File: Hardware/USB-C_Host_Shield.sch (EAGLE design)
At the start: 37 parts, among them U1 ARDUINO_UNO_R3_SHIELDBASIC, U3 74HC4050, U5 MAX3421, U6 3.3V/150mA

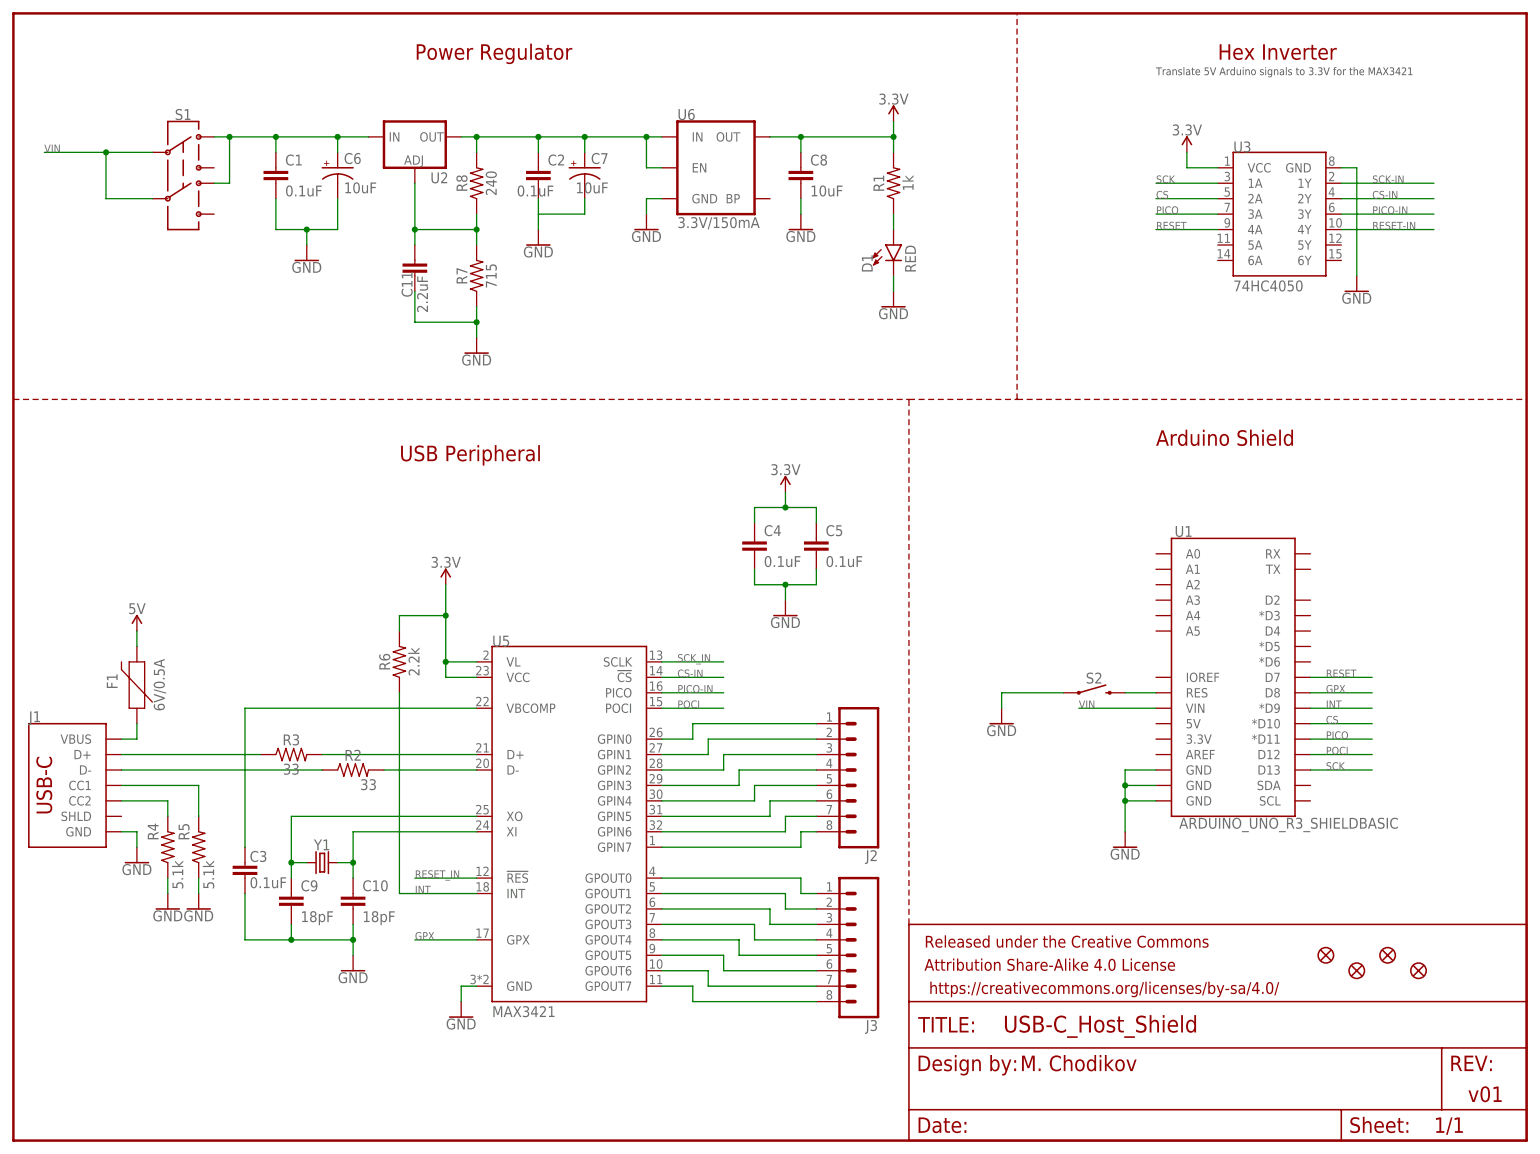
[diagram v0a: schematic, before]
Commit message: Continued with Layout
Adjusted resistors and components to all be 0603 size (besides caps with dielectrics). Placed components in sections so all capacitors and other components are in the right areas.
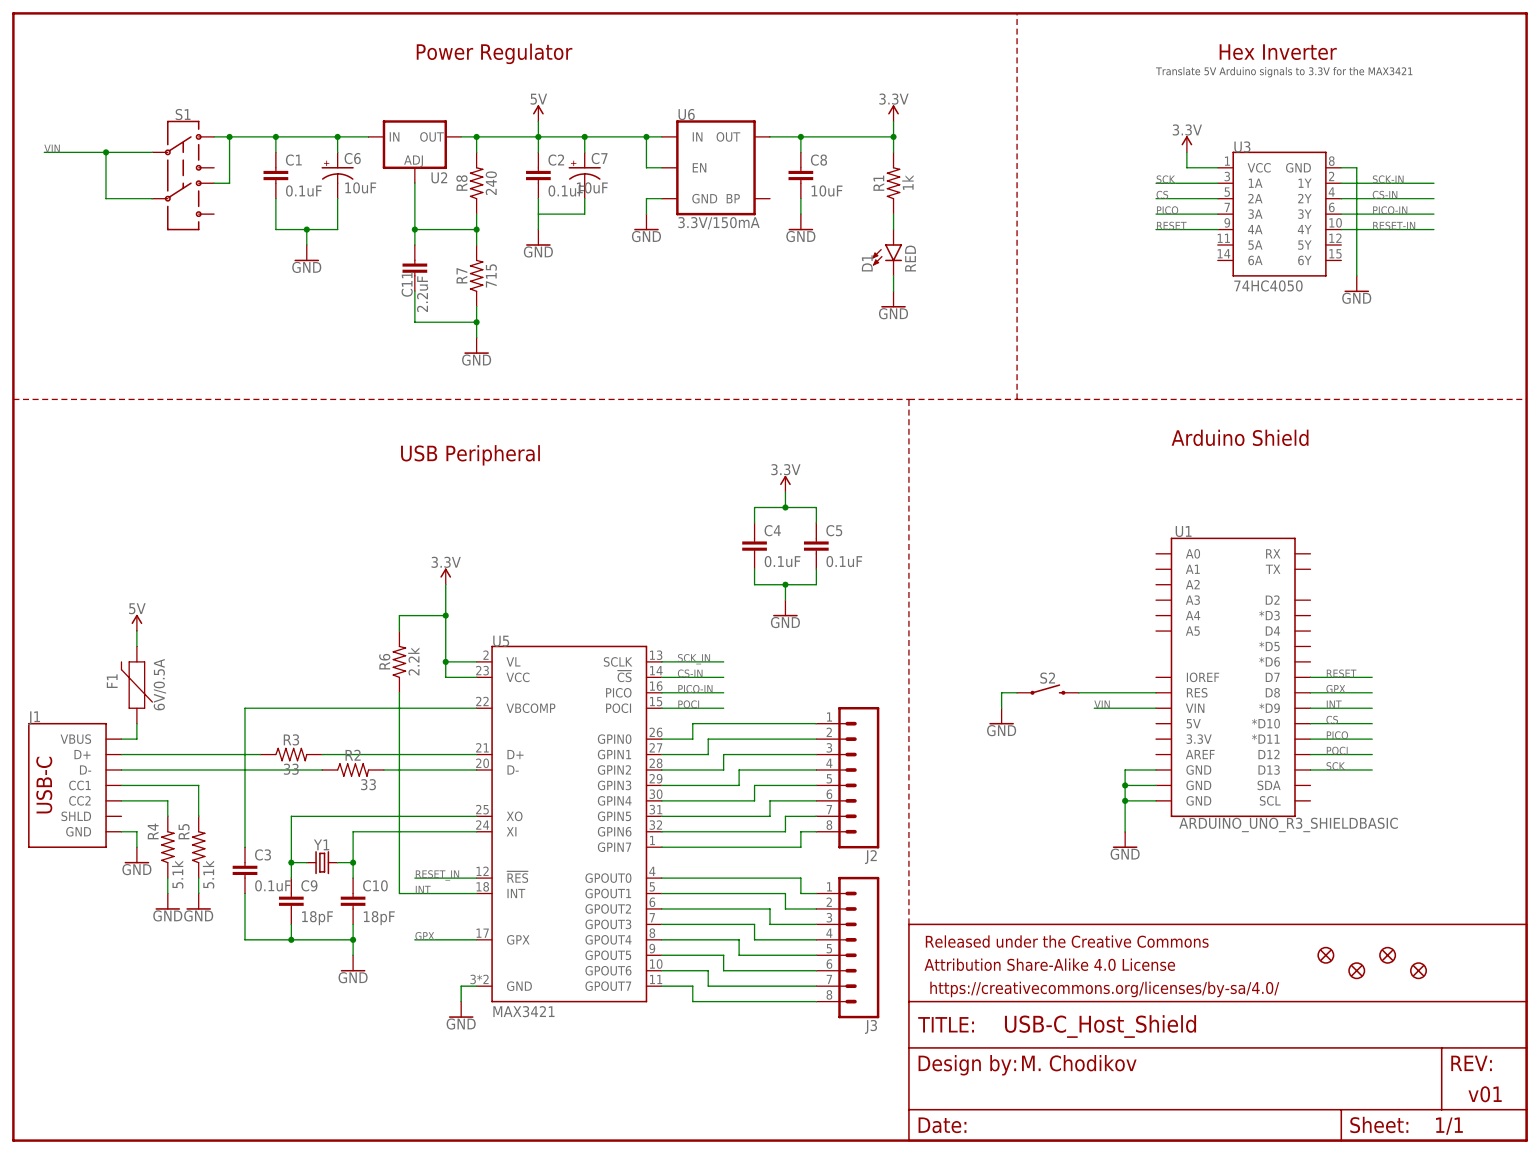
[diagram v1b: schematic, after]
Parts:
- C1, C2, C3, C4, C5: device SparkFun-Capacitors:0.1UF-0402T-6.3V-10%-X7R -> SparkFun-Capacitors:0.1UF-0603-25V-(+80/-20%)
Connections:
- net N$1 renamed D+
- net N$10 renamed MAX_D+
- net N$11 renamed D-
- net N$12 renamed GPOUT0
- net N$13 renamed GPOUT1
- net N$14 renamed GPOUT2
- net N$15 renamed CC1
- net N$16 renamed CC2
- net N$17 renamed GPOUT3
- net N$18 renamed GPOUT4
- net N$19 renamed GPOUT5
- net N$20 renamed GPOUT6
- net N$21 renamed GPOUT7
- net N$22 renamed GPIN7
- net N$23 renamed GPIN6
- net N$24 renamed GPIN5
- net N$25 renamed GPIN4
- net N$26 renamed GPIN3
- net N$27 renamed GPIN2
- net N$28 renamed GPIN1
- net N$29 renamed GPIN0
- net N$31 renamed VBUS
- net N$34 renamed XO
- net N$36 renamed XI
- net N$37 renamed VBCOMP
- net N$9 renamed MAX_D-
- removed net N$3: C2.1, C7.+, R8.2, U2.OUT, U6.EN, U6.IN
- net 5V: now also C2.1, C7.+, R8.2, U2.OUT, U6.EN, U6.IN
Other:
- moved on the sheet: S2

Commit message: Updated for Diff Pair Routing
Updated the layer stackup and net classes for differential pair routing. Changed in both schematic and layout. Routed sensitive signals
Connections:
- net D+ renamed D_P
- net D- renamed D_N
- net MAX_D+ renamed MAX_D_P
- net MAX_D- renamed MAX_D_N
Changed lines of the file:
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@@
 <class number="1" name="VIN" width="0" drill="0">
+</class>
+<class number="2" name="diff pairs" width="0.0889" drill="0">
 </class>
 </classes>
@@
 </segment>
 </net>
-<net name="D+" class="0">
+<net name="D_P" class="2">
 <segment>
 <pinref part="J1" gate="J1" pin="D+"/>
 <pinref part="R3" gate="G$1" pin="1"/>
 <wire x1="17.78" y1="63.5" x2="40.64" y2="63.5" width="0.1524" layer="91"/>
-</segment>
-</net>
-<net name="D-" class="0">
+<label x="25.4" y="63.5" size="1.27" layer="95"/>
+</segment>
+</net>
+<net name="D_N" class="2">
 <segment>
 <pinref part="R2" gate="G$1" pin="1"/>
 <pinref part="J1" gate="J1" pin="D-"/>
 <wire x1="50.8" y1="60.96" x2="17.78" y2="60.96" width="0.1524" layer="91"/>
-</segment>
-</net>
-<net name="MAX_D-" class="0">
+<label x="25.4" y="60.96" size="1.27" layer="95"/>
+</segment>
+</net>
+<net name="MAX_D_N" class="0">
 <segment>
 <pinref part="R2" gate="G$1" pin="2"/>
 <pinref part="U5" gate="G$1" pin="D-"/>
 <wire x1="60.96" y1="60.96" x2="76.2" y2="60.96" width="0.1524" layer="91"/>
-</segment>
-</net>
-<net name="MAX_D+" class="0">
+<label x="66.04" y="60.96" size="1.27" layer="95"/>
+</segment>
+</net>
+<net name="MAX_D_P" class="0">
 <segment>
 <pinref part="R3" gate="G$1" pin="2"/>
 <pinref part="U5" gate="G$1" pin="D+"/>
 <wire x1="50.8" y1="63.5" x2="76.2" y2="63.5" width="0.1524" layer="91"/>
-</segment>
-</net>
+<label x="66.04" y="63.5" size="1.27" layer="95"/>
+</segment>
+</net>

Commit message: Continued Layout
Continued with layout, added GND polygons - need to finish airwires and creating keepout layers
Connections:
- removed net SCK_IN: U5.SCLK
- net SCK-IN: now also U5.SCLK
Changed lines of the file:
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@@
-</segment>
-</net>
-<net name="SCK_IN" class="0">
-<segment>
-<pinref part="U5" gate="G$1" pin="SCLK"/>
-<wire x1="106.68" y1="78.74" x2="116.84" y2="78.74" width="0.1524" layer="91"/>
-<label x="109.22" y="78.74" size="1.27" layer="95"/>
 </segment>
 </net>
@@
 <label x="223.52" y="157.48" size="1.27" layer="95"/>
 </segment>
+<segment>
+<pinref part="U5" gate="G$1" pin="SCLK"/>
+<wire x1="106.68" y1="78.74" x2="116.84" y2="78.74" width="0.1524" layer="91"/>
+<label x="109.22" y="78.74" size="1.27" layer="95"/>
+</segment>
 </net>

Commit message: Approved and worked through errors
Worked through and approved many ERC and DRC Errors. Ready for design review.
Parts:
- J1: value (none) -> USB-C
- J2: value (none) -> GPIN
- J3: value (none) -> GPOUT
- S1: value (none) -> POWER-ON
- U2: value (none) -> LM1117
- Y1: value (none) -> 12.0mhZ
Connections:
- removed net N$5: C11.2, R7.1
- removed net N$6: C2.2, C7.-
- removed net N$8: D1.C
- removed net RESET_IN: U5.!RES
- net GND: now also C11.2, C2.2, C7.-, D1.C, R7.1
- net RESET-IN: now also U5.!RES
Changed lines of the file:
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@@
 <part name="FD4" library="SparkFun-Aesthetics" deviceset="FIDUCIAL" device="UFIDUCIAL"/>
 <part name="U1" library="SparkFun-Boards" deviceset="ARDUINO_UNO_R3_SHIELD" device="BASIC"/>
-<part name="J1" library="SparkFun-Connectors" deviceset="USB_C" device="_2-LAYER_PADS"/>
-<part name="S1" library="SparkFun-Switches" deviceset="SWITCH-DPDT" device="-SMD-AYZ0202"/>
-<part name="U2" library="SparkFun-IC-Power" deviceset="V_REG_LM1117" device="SOT223"/>
+<part name="J1" library="SparkFun-Connectors" deviceset="USB_C" device="_2-LAYER_PADS" value="USB-C"/>
+<part name="S1" library="SparkFun-Switches" deviceset="SWITCH-DPDT" device="-SMD-AYZ0202" value="POWER-ON"/>
+<part name="U2" library="SparkFun-IC-Power" deviceset="V_REG_LM1117" device="SOT223" value="LM1117"/>
 <part name="SUPPLY1" library="SparkFun-PowerSymbols" deviceset="3.3V" device=""/>
 <part name="GND1" library="SparkFun-PowerSymbols" deviceset="GND" device=""/>
@@
 <part name="GND8" library="SparkFun-PowerSymbols" deviceset="GND" device=""/>
 <part name="GND9" library="SparkFun-PowerSymbols" deviceset="GND" device=""/>
-<part name="J2" library="SparkFun-Connectors" deviceset="CONN_08" device="&quot;"/>
-<part name="J3" library="SparkFun-Connectors" deviceset="CONN_08" device="&quot;"/>
+<part name="J2" library="SparkFun-Connectors" deviceset="CONN_08" device="&quot;" value="GPIN"/>
+<part name="J3" library="SparkFun-Connectors" deviceset="CONN_08" device="&quot;" value="GPOUT"/>
 <part name="SUPPLY4" library="SparkFun-PowerSymbols" deviceset="3.3V" device=""/>
 <part name="C9" library="SparkFun-Capacitors" deviceset="18PF" device="-0603-50V-5%" value="18pF"/>
 <part name="C10" library="SparkFun-Capacitors" deviceset="18PF" device="-0603-50V-5%" value="18pF"/>
-<part name="Y1" library="SparkFun-Clocks" deviceset="CRYSTAL-12MHZ" device=""/>
+<part name="Y1" library="SparkFun-Clocks" deviceset="CRYSTAL-12MHZ" device="" value="12.0mhZ"/>
 <part name="GND10" library="SparkFun-PowerSymbols" deviceset="GND" device=""/>
 <part name="R4" library="SparkFun-Resistors" deviceset="5.1KOHM" device="5.1KOHM-0603-1/10W-1%" value="5.1k"/>
@@
 <instance part="U2" gate="G$1" x="66.04" y="165.1" smashed="yes">
 <attribute name="NAME" x="68.58" y="157.48" size="1.778" layer="95"/>
-<attribute name="VALUE" x="68.58" y="154.94" size="1.778" layer="96"/>
+<attribute name="VALUE" x="61.214" y="168.148" size="1.778" layer="96"/>
 </instance>
 <instance part="SUPPLY1" gate="G$1" x="127" y="106.68" smashed="yes">
@@
 </instance>
 <instance part="Y1" gate="G$1" x="50.8" y="45.72" smashed="yes">
-<attribute name="NAME" x="50.8" y="47.752" size="1.778" layer="95" font="vector" align="bottom-center"/>
-<attribute name="VALUE" x="50.8" y="43.688" size="1.778" layer="96" font="vector" align="top-center"/>
+<attribute name="NAME" x="50.8" y="50.292" size="1.778" layer="95" font="vector" align="bottom-center"/>
+<attribute name="VALUE" x="50.8" y="49.53" size="1.778" layer="96" font="vector" align="top-center"/>
 </instance>
 <instance part="GND10" gate="1" x="55.88" y="27.94" smashed="yes">
@@
 <pinref part="GND15" gate="1" pin="GND"/>
 </segment>
-</net>
-<net name="N$6" class="0">
+<segment>
+<pinref part="D1" gate="G$1" pin="C"/>
+<wire x1="144.78" y1="142.24" x2="144.78" y2="139.7" width="0.1524" layer="91"/>
+<pinref part="GND7" gate="1" pin="GND"/>
+</segment>
 <segment>
 <wire x1="86.36" y1="154.94" x2="86.36" y2="152.4" width="0.1524" layer="91"/>
+<pinref part="GND5" gate="1" pin="GND"/>
+<pinref part="C2" gate="G$1" pin="2"/>
 <pinref part="C7" gate="G$1" pin="-"/>
+<wire x1="86.36" y1="152.4" x2="86.36" y2="149.86" width="0.1524" layer="91"/>
 <wire x1="93.98" y1="152.4" x2="93.98" y2="154.94" width="0.1524" layer="91"/>
 <wire x1="93.98" y1="152.4" x2="86.36" y2="152.4" width="0.1524" layer="91"/>
-<wire x1="86.36" y1="152.4" x2="86.36" y2="149.86" width="0.1524" layer="91"/>
-<pinref part="GND5" gate="1" pin="GND"/>
-<pinref part="C2" gate="G$1" pin="2"/>
+<junction x="86.36" y="152.4"/>
+</segment>
+<segment>
+<pinref part="GND4" gate="1" pin="GND"/>
+<pinref part="R7" gate="G$1" pin="1"/>
+<wire x1="76.2" y1="137.16" x2="76.2" y2="134.62" width="0.1524" layer="91"/>
+<pinref part="C11" gate="G$1" pin="2"/>
+<wire x1="76.2" y1="134.62" x2="76.2" y2="132.08" width="0.1524" layer="91"/>
+<wire x1="66.04" y1="139.7" x2="66.04" y2="134.62" width="0.1524" layer="91"/>
+<wire x1="66.04" y1="134.62" x2="76.2" y2="134.62" width="0.1524" layer="91"/>
+<junction x="76.2" y="134.62"/>
 </segment>
 </net>
@@
 <wire x1="144.78" y1="152.4" x2="144.78" y2="149.86" width="0.1524" layer="91"/>
 <pinref part="R1" gate="G$1" pin="1"/>
-</segment>
-</net>
-<net name="N$8" class="0">
-<segment>
-<pinref part="D1" gate="G$1" pin="C"/>
-<wire x1="144.78" y1="142.24" x2="144.78" y2="139.7" width="0.1524" layer="91"/>
-<pinref part="GND7" gate="1" pin="GND"/>
 </segment>
 </net>
@@
 </segment>
 </net>
-<net name="N$5" class="0">
-<segment>
-<pinref part="GND4" gate="1" pin="GND"/>
-<pinref part="R7" gate="G$1" pin="1"/>
-<wire x1="76.2" y1="137.16" x2="76.2" y2="134.62" width="0.1524" layer="91"/>
-<pinref part="C11" gate="G$1" pin="2"/>
-<wire x1="76.2" y1="134.62" x2="76.2" y2="132.08" width="0.1524" layer="91"/>
-<wire x1="66.04" y1="139.7" x2="66.04" y2="134.62" width="0.1524" layer="91"/>
-<wire x1="66.04" y1="134.62" x2="76.2" y2="134.62" width="0.1524" layer="91"/>
-<junction x="76.2" y="134.62"/>
-</segment>
-</net>
 <net name="RESET" class="0">
 <segment>
@@
 <pinref part="U5" gate="G$1" pin="GPIN0"/>
 <wire x1="111.76" y1="66.04" x2="106.68" y2="66.04" width="0.1524" layer="91"/>
-</segment>
-</net>
-<net name="RESET_IN" class="0">
-<segment>
-<pinref part="U5" gate="G$1" pin="!RES"/>
-<wire x1="76.2" y1="43.18" x2="66.04" y2="43.18" width="0.1524" layer="91"/>
-<label x="66.04" y="43.18" size="1.27" layer="95"/>
 </segment>
 </net>
@@
 <label x="223.52" y="149.86" size="1.27" layer="95"/>
 </segment>
+<segment>
+<pinref part="U5" gate="G$1" pin="!RES"/>
+<wire x1="76.2" y1="43.18" x2="66.04" y2="43.18" width="0.1524" layer="91"/>
+<label x="66.04" y="43.18" size="1.27" layer="95"/>
+</segment>
 </net>
 <net name="N$1" class="0">
@@
 </sheet>
 </sheets>
+<errors>
+</errors>
 </schematic>
 </drawing>

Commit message: Adjusted design from comments
Added switch in schematic for swap between 5V and VIN from Arduino, added more GND vias and adjusted traces for GND pour, changed schematic tags to flags rather than text, adjusted version number on the back of the board
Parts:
- added S4: Power_Switch, SparkFun-Switches:SWITCH-SPDT-SMD-AYZ0202
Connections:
- new net N$5: S4.P, U6.EN, U6.IN
- new net N$6: C2.1, C7.+, R8.2, S4.O, U2.OUT
- net 5V: now also S4.S, U1.5V; no longer C2.1, C7.+, R8.2, U2.OUT, U6.EN, U6.IN
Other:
- moved on the sheet: C1, C11, C2, C6, C7, C8, D1, R1, R7, R8, S1, U2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

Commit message: Adjusted for design review
Many changes for design have been completed - NOT READY FOR ORDER. See "USB-C PT2" design review document for further information on what needs to be completed.
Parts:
- added JP1: JUMPER-SMT_2_NC_TRACE_SILK, SparkFun-Jumpers:JUMPER-SMT_2_NC_TRACE_SILK
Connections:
- new net N$8: J1.SHLD, JP1.2
- net GND: now also JP1.1
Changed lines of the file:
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@@
 <part name="SUPPLY6" library="SparkFun-PowerSymbols" deviceset="VIN" device=""/>
 <part name="SUPPLY9" library="SparkFun-PowerSymbols" deviceset="VIN" device=""/>
+<part name="GND16" library="SparkFun-PowerSymbols" deviceset="GND" device=""/>
+<part name="JP1" library="SparkFun-Jumpers" deviceset="JUMPER-SMT_2_NC_TRACE" device="_SILK" package3d_urn="urn:adsk.eagle:package:39281/1"/>
 </parts>
 <sheets>
@@
 <text x="165.608" y="11.43" size="2.54" layer="94">M. Chodikov</text>
 <text x="239.268" y="6.35" size="2.54" layer="94">v01</text>
-<text x="66.04" y="177.8" size="2.54" layer="94">Power Regulator</text>
-<text x="190.5" y="106.68" size="2.54" layer="94">Arduino Shield</text>
-<text x="63.5" y="104.14" size="2.54" layer="94">USB Peripheral</text>
+<text x="66.04" y="177.8" size="2.54" layer="94" font="vector">Power Regulator</text>
+<text x="190.5" y="106.68" size="2.54" layer="94" font="vector">Arduino Shield</text>
+<text x="63.5" y="104.14" size="2.54" layer="94" font="vector">USB Peripheral</text>
 <wire x1="0" y1="114.3" x2="147.32" y2="114.3" width="0.2032" layer="94" style="shortdash"/>
 <wire x1="147.32" y1="114.3" x2="165.1" y2="114.3" width="0.2032" layer="94" style="shortdash"/>
@@
 <wire x1="147.32" y1="35.56" x2="147.32" y2="114.3" width="0.2032" layer="94" style="shortdash"/>
 <wire x1="165.1" y1="114.3" x2="248.92" y2="114.3" width="0.2032" layer="94" style="shortdash"/>
-<text x="198.12" y="177.8" size="2.54" layer="94">Hex Inverter</text>
+<text x="198.12" y="177.8" size="2.54" layer="94" font="vector">Hex Inverter</text>
 <text x="187.96" y="175.26" size="1.27" layer="97">Translate 5V Arduino signals to 3.3V for the MAX3421</text>
 </plain>
@@
 <instance part="C2" gate="G$1" x="78.74" y="147.32" smashed="yes">
 <attribute name="NAME" x="80.264" y="150.241" size="1.778" layer="95" font="vector"/>
-<attribute name="VALUE" x="80.264" y="145.161" size="1.778" layer="96" font="vector"/>
+<attribute name="VALUE" x="75.184" y="145.161" size="1.778" layer="96" font="vector"/>
 </instance>
 <instance part="C1" gate="G$1" x="35.56" y="147.32" smashed="yes">
@@
 <instance part="SUPPLY9" gate="G$1" x="177.8" y="76.2" smashed="yes">
 <attribute name="VALUE" x="177.8" y="78.994" size="1.778" layer="96" font="vector" align="bottom-center"/>
+</instance>
+<instance part="GND16" gate="1" x="22.86" y="17.78" smashed="yes">
+<attribute name="VALUE" x="22.86" y="17.526" size="1.778" layer="96" font="vector" align="top-center"/>
+</instance>
+<instance part="JP1" gate="G$1" x="22.86" y="27.94" smashed="yes" rot="R90">
+<attribute name="NAME" x="19.812" y="27.94" size="1.778" layer="95" font="vector" rot="R90" align="center"/>
+<attribute name="VALUE" x="25.908" y="27.94" size="1.778" layer="96" font="vector" rot="R90" align="center" display="off"/>
 </instance>
 </instances>
@@
 <wire x1="58.42" y1="124.46" x2="68.58" y2="124.46" width="0.1524" layer="91"/>
 <junction x="68.58" y="124.46"/>
+</segment>
+<segment>
+<wire x1="22.86" y1="22.86" x2="22.86" y2="20.32" width="0.1524" layer="91"/>
+<pinref part="GND16" gate="1" pin="GND"/>
+<pinref part="JP1" gate="G$1" pin="1"/>
 </segment>
 </net>
@@
 </segment>
 </net>
+<net name="N$8" class="0">
+<segment>
+<pinref part="J1" gate="J1" pin="SHLD"/>
+<wire x1="17.78" y1="53.34" x2="22.86" y2="53.34" width="0.1524" layer="91"/>
+<wire x1="22.86" y1="53.34" x2="22.86" y2="33.02" width="0.1524" layer="91"/>
+<pinref part="JP1" gate="G$1" pin="2"/>
+</segment>
+</net>
 </nets>
 </sheet>
 </sheets>
-<errors>
-</errors>
 </schematic>
 </drawing>
@@
 will not be understood (or retained) with this version.
 </note>
+<note version="8.3" severity="warning">
+Since Version 8.3, EAGLE supports the association of 3D packages
+with devices in libraries, schematics, and board files. Those 3D
+packages will not be understood (or retained) with this version.
+</note>
 </compatibility>
